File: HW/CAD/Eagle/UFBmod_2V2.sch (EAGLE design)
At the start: 210 parts, among them J1411 ABRACON_ARJE-0034, T0551 MMBT2222, U0501 MIDAS_MCCOG21605B6W-FPTLWI, U0601 MAX5217, U0651 LM4120IM5-3.0, U0701 AT86RF215-ZU, U0711 ASVTX-13-D-26.000MHZ-I05-T, U0811 PE4259, U0821 RFX1010, U0881 B39871B3440U410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

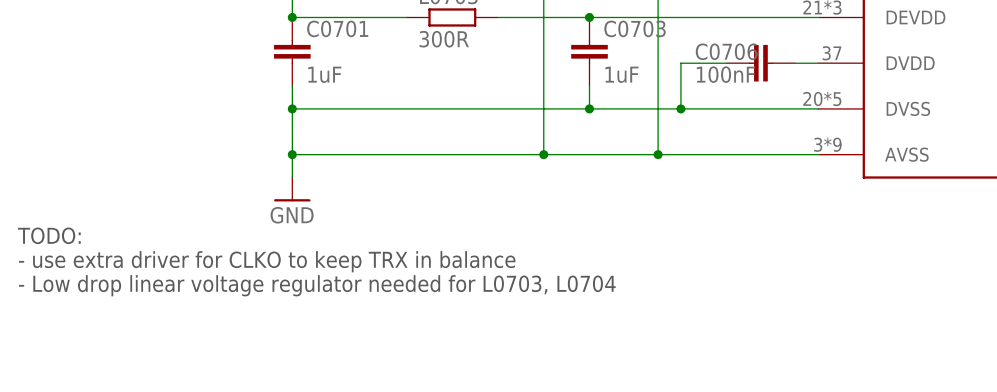
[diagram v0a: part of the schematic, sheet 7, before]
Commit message: HW - Eagle - V2.2 - remarks added for re-design of V2.2 near the TRX
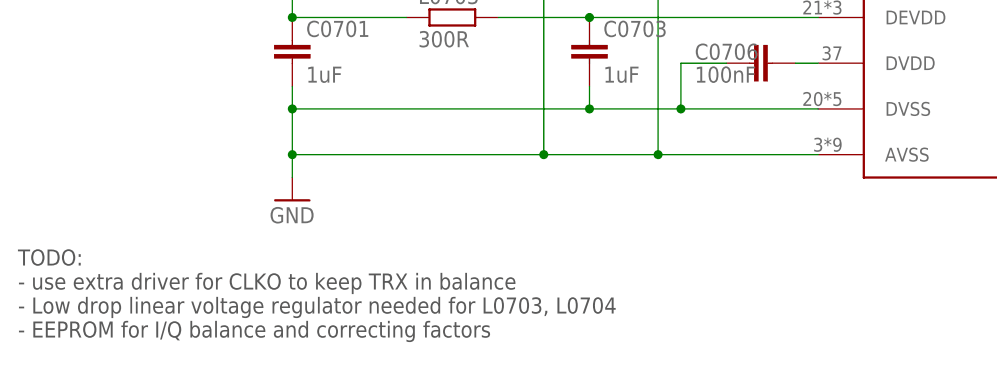
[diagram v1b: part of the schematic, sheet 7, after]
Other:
- note added: "TODO: - use extra driver for CLKO to keep TRX in balance - Low drop linear voltage regulator needed for L0703, L0704 - EEPROM for I/Q balance and correcting factors"
- note removed: "TODO: - use extra driver for CLKO to keep TRX in balance - Low drop linear voltage regulator needed for L0703, L0704"
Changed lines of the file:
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@@
 <text x="22.86" y="162.56" size="2.54" layer="97" ratio="15">Microchip Technologies AT86RF215</text>
 <text x="93.98" y="83.82" size="1.778" layer="97">26MHz</text>
-<text x="15.24" y="22.86" size="1.778" layer="97">TODO:
+<text x="15.24" y="17.78" size="1.778" layer="97">TODO:
 - use extra driver for CLKO to keep TRX in balance
-- Low drop linear voltage regulator needed for L0703, L0704</text>
+- Low drop linear voltage regulator needed for L0703, L0704
+- EEPROM for I/Q balance and correcting factors</text>
 </plain>
 <instances>

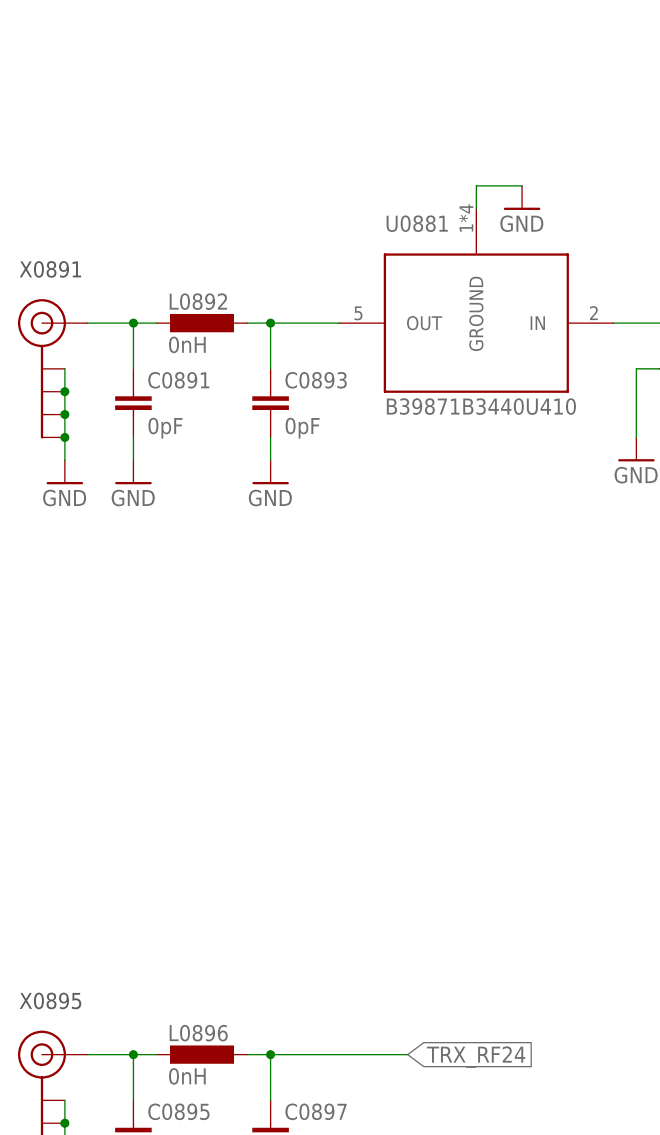
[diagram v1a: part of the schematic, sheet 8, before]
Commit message: HW - Eagle - V2.1 V2.2 - RF power level remarks  added
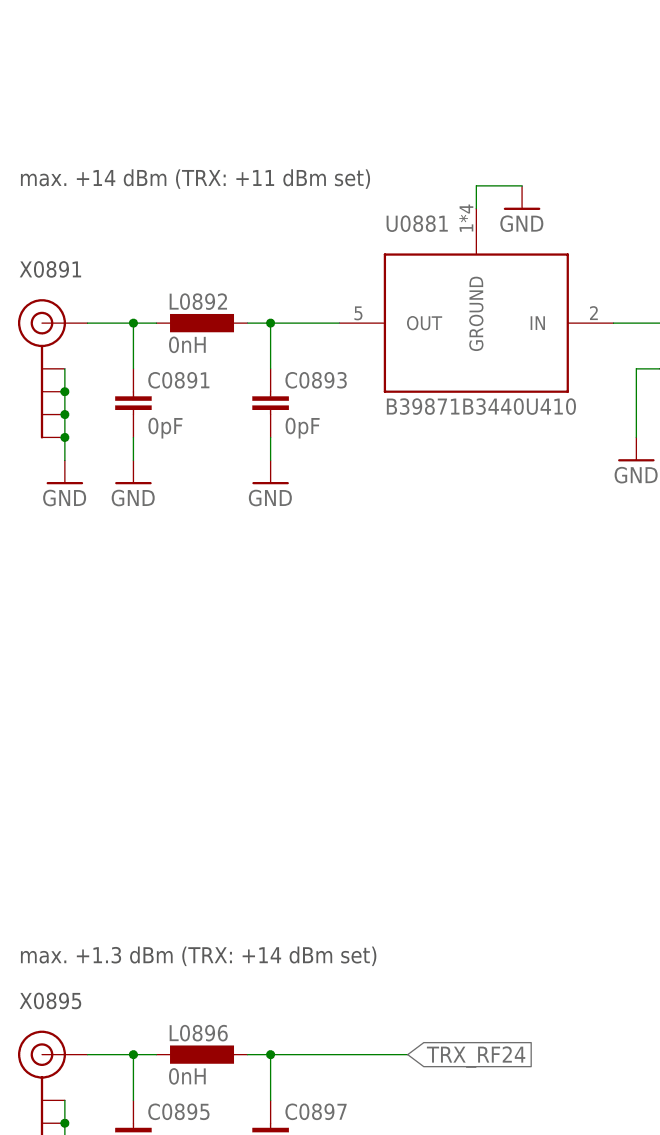
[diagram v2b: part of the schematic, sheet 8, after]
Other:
- note added: "max. +1.3 dBm (TRX: +14 dBm set)"
- note added: "max. +14 dBm (TRX: +11 dBm set)"
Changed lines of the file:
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@@
 <text x="7.62" y="121.92" size="1.778" layer="97">X0891</text>
 <text x="7.62" y="40.64" size="1.778" layer="97">X0895</text>
+<text x="7.62" y="45.72" size="1.778" layer="97">max. +1.3 dBm (TRX: +14 dBm set)</text>
+<text x="7.62" y="132.08" size="1.778" layer="97">max. +14 dBm (TRX: +11 dBm set)</text>
 </plain>
 <instances>

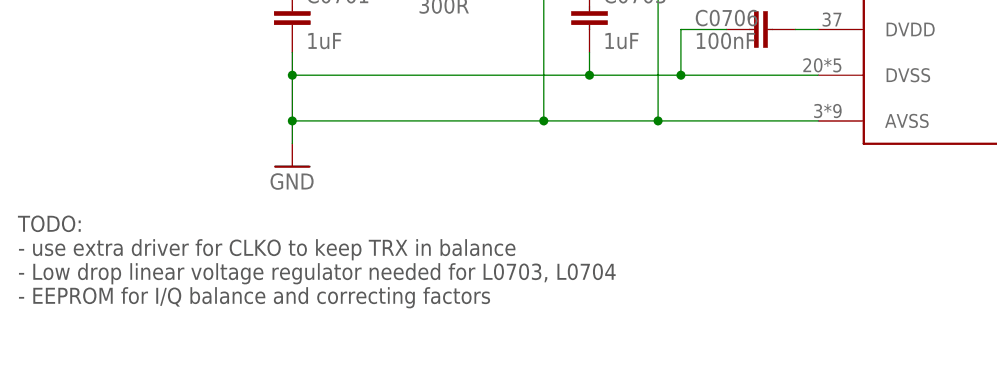
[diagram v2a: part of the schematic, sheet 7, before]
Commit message: HW - Eagle - V2.1 V2.2 - Remarks for RF09 BALUN replacement
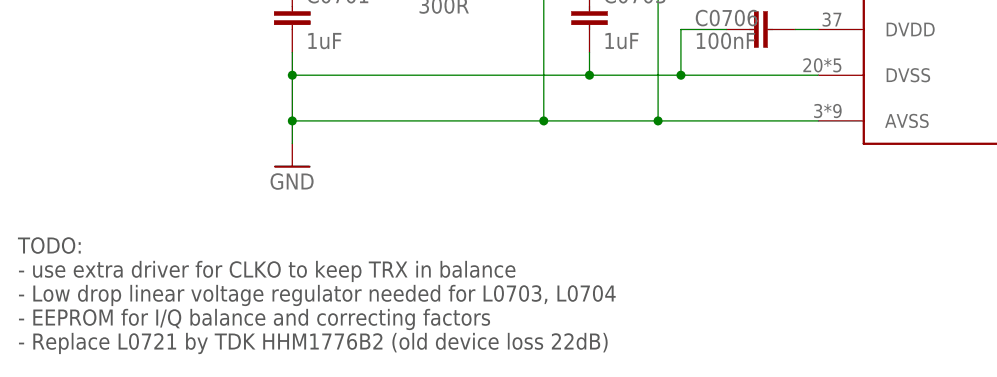
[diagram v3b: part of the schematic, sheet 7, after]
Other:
- note added: "TODO: - use extra driver for CLKO to keep TRX in balance - Low drop linear voltage regulator needed for L0703, L0704 - EEPROM for I/Q balance and correcting factors - Replace L0721 by TDK HHM1776B2 (old device loss 22dB)"
- note removed: "TODO: - use extra driver for CLKO to keep TRX in balance - Low drop linear voltage regulator needed for L0703, L0704 - EEPROM for I/Q balance and correcting factors"
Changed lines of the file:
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@@
 <text x="22.86" y="162.56" size="2.54" layer="97" ratio="15">Microchip Technologies AT86RF215</text>
 <text x="93.98" y="83.82" size="1.778" layer="97">26MHz</text>
-<text x="15.24" y="17.78" size="1.778" layer="97">TODO:
+<text x="15.24" y="12.7" size="1.778" layer="97">TODO:
 - use extra driver for CLKO to keep TRX in balance
 - Low drop linear voltage regulator needed for L0703, L0704
-- EEPROM for I/Q balance and correcting factors</text>
+- EEPROM for I/Q balance and correcting factors
+- Replace L0721 by TDK HHM1776B2 (old device loss 22dB)</text>
 </plain>
 <instances>

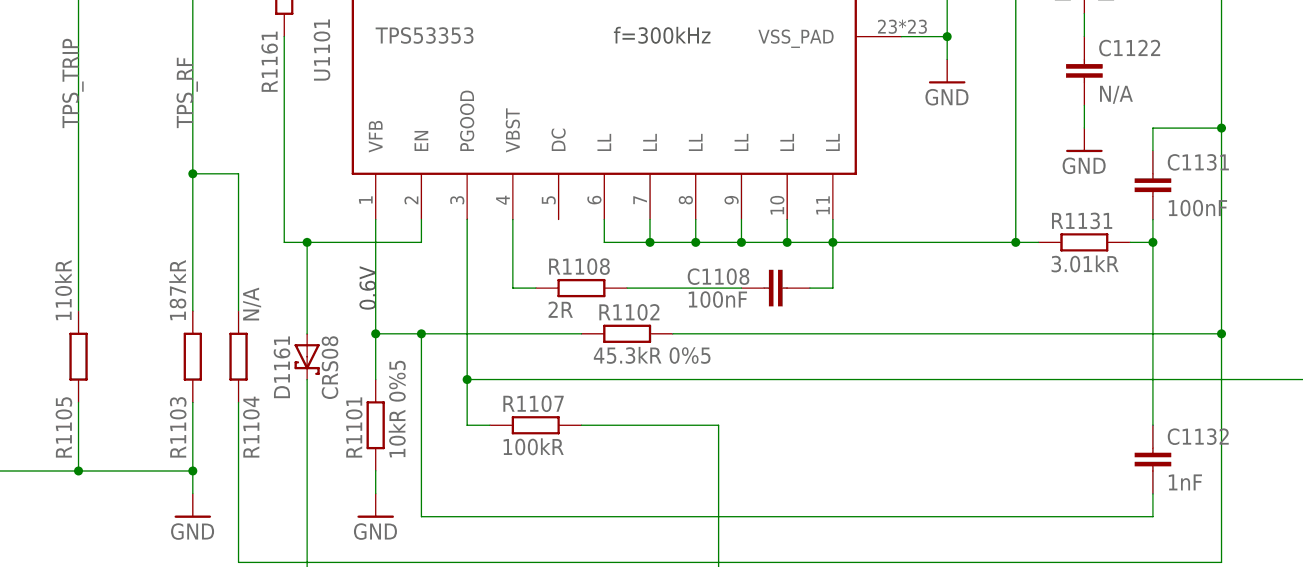
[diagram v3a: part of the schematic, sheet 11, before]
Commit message: HW - Eagle - V2.1 V2.2 - PMIC values changed for lower swing at VFB and OV-protection
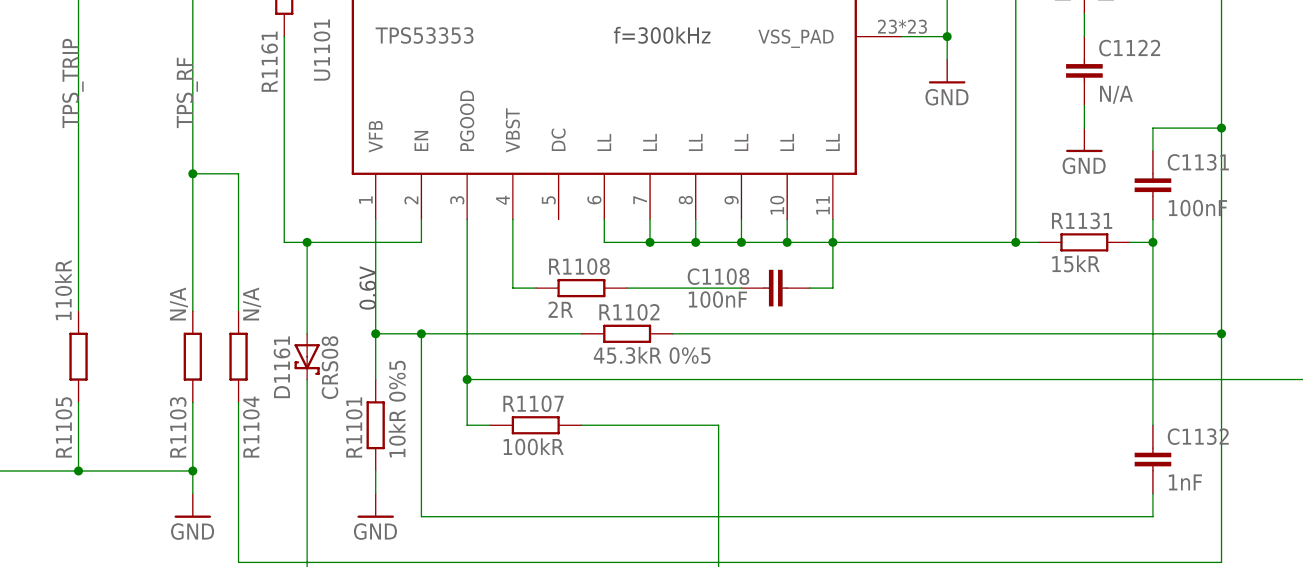
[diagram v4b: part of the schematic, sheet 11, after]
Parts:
- R1103: value 187kR -> N/A
- R1131: value 3.01kR -> 15kR
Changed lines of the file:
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@@
 <part name="C1102" library="df4iah_rcl" deviceset="C-EU" device="C0402" value="1uF"/>
 <part name="C1111" library="df4iah_rcl" deviceset="C-EU" device="C0805" value="22uF"/>
-<part name="R1103" library="df4iah_rcl" deviceset="R-EU_" device="R0402" value="187kR"/>
+<part name="R1103" library="df4iah_rcl" deviceset="R-EU_" device="R0402" value="N/A"/>
 <part name="R1104" library="df4iah_rcl" deviceset="R-EU_" device="R0402" value="N/A">
 <variant name="Std" populate="no"/>
@@
 <variant name="Std" populate="no"/>
 </part>
-<part name="R1131" library="df4iah_rcl" deviceset="R-EU_" device="R0402" value="3.01kR"/>
+<part name="R1131" library="df4iah_rcl" deviceset="R-EU_" device="R0402" value="15kR"/>
 <part name="C1131" library="df4iah_rcl" deviceset="C-EU" device="C0402" value="100nF"/>
 <part name="C1132" library="df4iah_rcl" deviceset="C-EU" device="C0402" value="1nF"/>
